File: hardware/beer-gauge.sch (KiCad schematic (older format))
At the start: 10 parts

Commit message: Created TEENSY footprint
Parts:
- added W? (x5): TEST_1P, symbol TEST_1P
- U?: footprint MODULE -> TEENSY:TEENSY
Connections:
- net labels added: TOUCH_DOWN, TOUCH_LEFT, TOUCH_RIGHT, TOUCH_SEL, TOUCH_UP
- wire segments 94 -> 114
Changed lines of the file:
@@
 F 0 "U?" H 3750 2100 50  0000 C CNN
 F 1 "TEENSY_3.2" H 3750 2300 50  0000 C CNN
-F 2 "MODULE" H 3750 2200 50  0001 C CNN
+F 2 "TEENSY:TEENSY" H 3750 2200 50  0001 C CNN
 F 3 "DOCUMENTATION" H 3750 2200 50  0001 C CNN
 	1    3750 2200
@@
 Wire Wire Line
 	8100 2450 8100 2400
-Text Label 1150 1750 0    60   ~ 0
+Text Label 2300 1650 0    60   ~ 0
 SCALE_GAIN0
-Text Label 1150 1850 0    60   ~ 0
+Text Label 2300 1750 0    60   ~ 0
 SCALE_GAIN1
 Text Label 2250 2850 0    60   ~ 0
@@
 Text Label 5300 2750 2    60   ~ 0
 SCALE_SCLK
-Text Label 1150 2150 0    60   ~ 0
+Text Label 2300 1850 0    60   ~ 0
 SCALE_PWDN
-Text Label 1150 2250 0    60   ~ 0
+Text Label 2300 1950 0    60   ~ 0
 SCALE_SPEED
-Text Label 1150 2350 0    60   ~ 0
+Text Label 2300 2050 0    60   ~ 0
 SCALE_A0
-Text Label 1150 2450 0    60   ~ 0
+Text Label 2300 2150 0    60   ~ 0
 SCALE_A1
 Wire Wire Line
@@
 Wire Wire Line
 	4450 5950 4450 5900
-Text Label 1150 2700 0    60   ~ 0
+Text Label 5300 2150 2    60   ~ 0
 DISP_RESET
 Text Label 5300 2250 2    60   ~ 0
@@
 Wire Wire Line
 	4500 2250 5300 2250
+$Comp
+L TEST_1P W?
+U 1 1 575F5A41
+P 7050 5500
+F 0 "W?" H 7050 5770 50  0000 C CNN
+F 1 "TEST_1P" H 7050 5700 50  0000 C CNN
+F 2 "" H 7250 5500 50  0000 C CNN
+F 3 "" H 7250 5500 50  0000 C CNN
+	1    7050 5500
+	0    -1   -1   0
+$EndComp
+$Comp
+L TEST_1P W?
+U 1 1 575F5ABE
+P 6450 6100
+F 0 "W?" H 6450 6370 50  0000 C CNN
+F 1 "TEST_1P" H 6450 6300 50  0000 C CNN
+F 2 "" H 6650 6100 50  0000 C CNN
+F 3 "" H 6650 6100 50  0000 C CNN
+	1    6450 6100
+	1    0    0    -1
+$EndComp
+$Comp
+L TEST_1P W?
+U 1 1 575F5BDB
+P 5800 5500
+F 0 "W?" H 5800 5770 50  0000 C CNN
+F 1 "TEST_1P" H 5800 5700 50  0000 C CNN
+F 2 "" H 6000 5500 50  0000 C CNN
+F 3 "" H 6000 5500 50  0000 C CNN
+	1    5800 5500
+	0    1    1    0
+$EndComp
+$Comp
+L TEST_1P W?
+U 1 1 575F5C18
+P 6550 5500
+F 0 "W?" H 6550 5770 50  0000 C CNN
+F 1 "TEST_1P" H 6550 5700 50  0000 C CNN
+F 2 "" H 6750 5500 50  0000 C CNN
+F 3 "" H 6750 5500 50  0000 C CNN
+	1    6550 5500
+	0    -1   -1   0
+$EndComp
+$Comp
+L TEST_1P W?
+U 1 1 575F5C61
+P 6450 4900
+F 0 "W?" H 6450 5170 50  0000 C CNN
+F 1 "TEST_1P" H 6450 5100 50  0000 C CNN
+F 2 "" H 6650 4900 50  0000 C CNN
+F 3 "" H 6650 4900 50  0000 C CNN
+	1    6450 4900
+	-1   0    0    1
+$EndComp
+Text Label 5200 5500 0    60   ~ 0
+TOUCH_LEFT
+Wire Wire Line
+	5200 5500 5800 5500
+Text Label 7700 5500 2    60   ~ 0
+TOUCH_RIGHT
+Wire Wire Line
+	7050 5500 7700 5500
+Text Label 5900 4850 0    60   ~ 0
+TOUCH_UP
+Wire Wire Line
+	5900 4850 6450 4850
+Wire Wire Line
+	6450 4850 6450 4900
+Text Label 5800 6250 0    60   ~ 0
+TOUCH_DOWN
+Wire Wire Line
+	5800 6250 6450 6250
+Wire Wire Line
+	6450 6250 6450 6100
+Text Label 7150 5300 2    60   ~ 0
+TOUCH_SEL
+Wire Wire Line
+	7150 5300 6550 5300
+Wire Wire Line
+	6550 5300 6550 5500
+Text Label 5300 1850 2    60   ~ 0
+TOUCH_UP
+Text Label 5300 1950 2    60   ~ 0
+TOUCH_DOWN
+Text Label 5300 2450 2    60   ~ 0
+TOUCH_LEFT
+Text Label 5300 2550 2    60   ~ 0
+TOUCH_RIGHT
+Text Label 5300 2650 2    60   ~ 0
+TOUCH_SEL
+Wire Wire Line
+	4500 2450 5300 2450
+Wire Wire Line
+	4500 2550 5300 2550
+Wire Wire Line
+	4500 2650 5300 2650
+Wire Wire Line
+	4500 2150 5300 2150
+Wire Wire Line
+	4500 1850 5300 1850
+Wire Wire Line
+	4500 1950 5300 1950
+Wire Wire Line
+	2300 1650 3000 1650
+Wire Wire Line
+	2300 1750 3000 1750
+Wire Wire Line
+	2300 1850 3000 1850
+Wire Wire Line
+	2300 1950 3000 1950
+Wire Wire Line
+	2300 2050 3000 2050
+Wire Wire Line
+	2300 2150 3000 2150
 $EndSCHEMATC

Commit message: Added subsheet for TEENSY schematic.  Working on TEENSY circuit based on online reference design.
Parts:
- removed U?: TEENSY_3.2, TEENSY:TEENSY, symbol TEENSY_3.2
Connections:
- wire segments 114 -> 134
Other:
- moved on the sheet: C?, IC?, P?, U?, W?

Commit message: Working on schematic
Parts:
- removed W? (x5): TEST_1P, symbol TEST_1P
- added C2: 0.1u, symbol C
- added D1: LED, symbol LED
- added R1: 470, symbol R
- added TP1, TP2, TP3, TP4, TP5: TOUCH_PAD, symbol TOUCH_PAD
- C3: renamed from C?; footprint (none) -> Capacitors_SMD:C_0603
- gave numbers to parts that had none: 8
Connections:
- wire segments 134 -> 110
- no-connect marks 6 -> 5
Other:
- moved on the sheet: C1, C3, C4, P1, P2, P3, P4, U1, U2

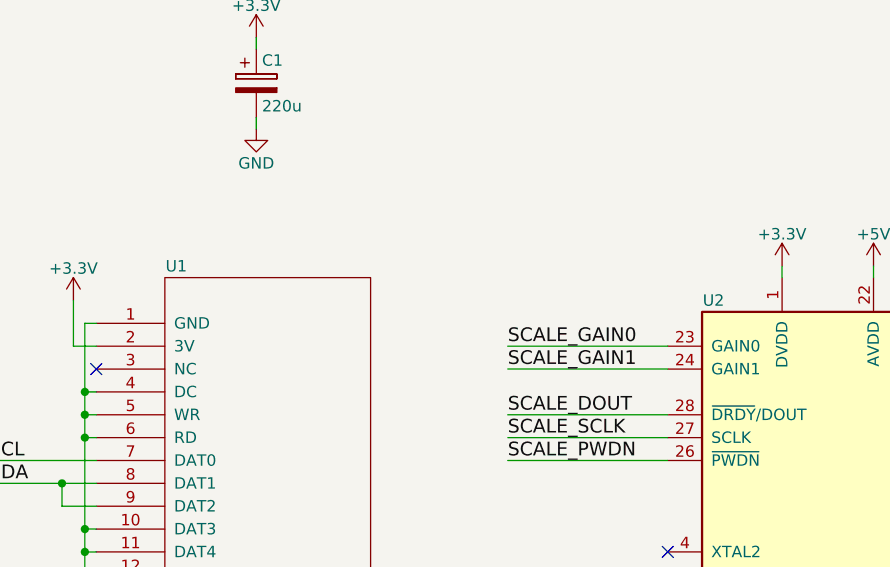
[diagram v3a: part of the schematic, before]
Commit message: Created schematic PDF.  Working on BOM.
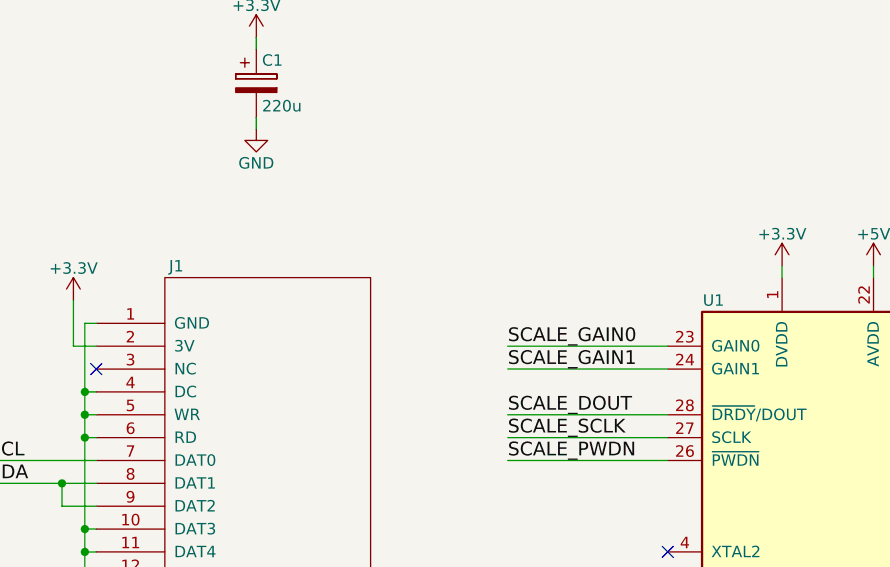
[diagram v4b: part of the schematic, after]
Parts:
- renumbered U1 to J1, U2 to U1
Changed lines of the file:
@@
 $EndDescr
 $Comp
-L ADS1234IPW U2
+L ADS1234IPW U1
 U 1 1 575B8EE8
 P 8000 3300
-F 0 "U2" H 8500 4400 50  0000 C CNN
+F 0 "U1" H 8500 4400 50  0000 C CNN
 F 1 "ADS1234IPW" H 7300 2200 50  0000 L CNN
 F 2 "" H 8000 3300 50  0000 C CIN
@@
 SCALE_A1
 $Comp
-L OLED_MODULE U1
+L OLED_MODULE J1
 U 1 1 575BBA3C
 P 5550 3250
-F 0 "U1" H 5150 4450 50  0000 C CNN
+F 0 "J1" H 5150 4450 50  0000 C CNN
 F 1 "OLED_MODULE" H 5350 2050 50  0000 C CNN
 F 2 "MODULE" H 5550 3250 50  0001 C CNN

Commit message: Working on BOM.
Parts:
- C1: footprint (none) -> Capacitors_SMD:c_elec_6.3x5.8
- C2, C4: footprint (none) -> Capacitors_SMD:C_0603
- D1: footprint (none) -> LEDs:LED_0603
- R1: footprint (none) -> Resistors_SMD:R_0603
- U1: footprint (none) -> Housings_SSOP:TSSOP-28_4.4x9.7mm_Pitch0.65mm
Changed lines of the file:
@@
 F 0 "U1" H 8500 4400 50  0000 C CNN
 F 1 "ADS1234IPW" H 7300 2200 50  0000 L CNN
-F 2 "" H 8000 3300 50  0000 C CIN
+F 2 "Housings_SSOP:TSSOP-28_4.4x9.7mm_Pitch0.65mm" H 8000 3300 50  0001 C CIN
 F 3 "" H 8000 3300 50  0000 C CNN
 	1    8000 3300
@@
 $EndComp
 $Comp
-L +5V #PWR01
+L +5V #PWR16
 U 1 1 575B9063
 P 9600 2400
-F 0 "#PWR01" H 9600 2250 50  0001 C CNN
+F 0 "#PWR16" H 9600 2250 50  0001 C CNN
 F 1 "+5V" H 9600 2540 50  0000 C CNN
 F 2 "" H 9600 2400 50  0000 C CNN
@@
 $EndComp
 $Comp
-L +3.3V #PWR02
+L +3.3V #PWR7
 U 1 1 575B907B
 P 7800 2050
-F 0 "#PWR02" H 7800 1900 50  0001 C CNN
+F 0 "#PWR7" H 7800 1900 50  0001 C CNN
 F 1 "+3.3V" H 7800 2190 50  0000 C CNN
 F 2 "" H 7800 2050 50  0000 C CNN
@@
 $EndComp
 $Comp
-L GND #PWR03
+L GND #PWR8
 U 1 1 575B9093
 P 8000 4600
-F 0 "#PWR03" H 8000 4350 50  0001 C CNN
+F 0 "#PWR8" H 8000 4350 50  0001 C CNN
 F 1 "GND" H 8000 4450 50  0000 C CNN
 F 2 "" H 8000 4600 50  0000 C CNN
@@
 $EndComp
 $Comp
-L GND #PWR04
+L GND #PWR17
 U 1 1 575B9815
 P 9700 4400
-F 0 "#PWR04" H 9700 4150 50  0001 C CNN
+F 0 "#PWR17" H 9700 4150 50  0001 C CNN
 F 1 "GND" H 9700 4250 50  0000 C CNN
 F 2 "" H 9700 4400 50  0000 C CNN
@@
 $EndComp
 $Comp
-L GND #PWR05
+L GND #PWR11
 U 1 1 575B9A5F
 P 8850 4300
-F 0 "#PWR05" H 8850 4050 50  0001 C CNN
+F 0 "#PWR11" H 8850 4050 50  0001 C CNN
 F 1 "GND" H 8850 4150 50  0000 C CNN
 F 2 "" H 8850 4300 50  0000 C CNN
@@
 $EndComp
 $Comp
-L +5V #PWR06
+L +5V #PWR10
 U 1 1 575BA1FA
 P 8750 2300
-F 0 "#PWR06" H 8750 2150 50  0001 C CNN
+F 0 "#PWR10" H 8750 2150 50  0001 C CNN
 F 1 "+5V" H 8750 2440 50  0000 C CNN
 F 2 "" H 8750 2300 50  0000 C CNN
@@
 $EndComp
 $Comp
-L +5V #PWR07
+L +5V #PWR9
 U 1 1 575BA2EA
 P 8200 2050
-F 0 "#PWR07" H 8200 1900 50  0001 C CNN
+F 0 "#PWR9" H 8200 1900 50  0001 C CNN
 F 1 "+5V" H 8200 2190 50  0000 C CNN
 F 2 "" H 8200 2050 50  0000 C CNN
@@
 F 0 "C4" H 9225 1800 50  0000 L CNN
 F 1 "0.1u" H 9225 1600 50  0000 L CNN
-F 2 "" H 9238 1550 50  0000 C CNN
+F 2 "Capacitors_SMD:C_0603" H 9238 1550 50  0001 C CNN
 F 3 "" H 9200 1700 50  0000 C CNN
 	1    9200 1700
@@
 $EndComp
 $Comp
-L +5V #PWR08
+L +5V #PWR14
 U 1 1 575BA474
 P 9200 1500
-F 0 "#PWR08" H 9200 1350 50  0001 C CNN
+F 0 "#PWR14" H 9200 1350 50  0001 C CNN
 F 1 "+5V" H 9200 1640 50  0000 C CNN
 F 2 "" H 9200 1500 50  0000 C CNN
@@
 $EndComp
 $Comp
-L GND #PWR09
+L GND #PWR15
 U 1 1 575BA4B7
 P 9200 1900
-F 0 "#PWR09" H 9200 1650 50  0001 C CNN
+F 0 "#PWR15" H 9200 1650 50  0001 C CNN
 F 1 "GND" H 9200 1750 50  0000 C CNN
 F 2 "" H 9200 1900 50  0000 C CNN
@@
 $EndComp
 $Comp
-L GND #PWR010
+L GND #PWR6
 U 1 1 575BA95F
 P 7250 4300
-F 0 "#PWR010" H 7250 4050 50  0001 C CNN
+F 0 "#PWR6" H 7250 4050 50  0001 C CNN
 F 1 "GND" H 7250 4150 50  0000 C CNN
 F 2 "" H 7250 4300 50  0000 C CNN
@@
 $EndComp
 $Comp
-L GND #PWR011
+L GND #PWR3
 U 1 1 575BBEBC
 P 4750 4300
-F 0 "#PWR011" H 4750 4050 50  0001 C CNN
+F 0 "#PWR3" H 4750 4050 50  0001 C CNN
 F 1 "GND" H 4750 4150 50  0000 C CNN
 F 2 "" H 4750 4300 50  0000 C CNN
@@
 NoConn ~ 4800 2500
 $Comp
-L +3.3V #PWR012
+L +3.3V #PWR2
 U 1 1 575BC1B4
 P 4700 2200
-F 0 "#PWR012" H 4700 2050 50  0001 C CNN
+F 0 "#PWR2" H 4700 2050 50  0001 C CNN
 F 1 "+3.3V" H 4700 2340 50  0000 C CNN
 F 2 "" H 4700 2200 50  0000 C CNN
@@
 F 0 "C1" H 5525 1350 50  0000 L CNN
 F 1 "220u" H 5525 1150 50  0000 L CNN
-F 2 "" H 5538 1100 50  0000 C CNN
+F 2 "Capacitors_SMD:c_elec_6.3x5.8" H 5538 1100 50  0001 C CNN
 F 3 "" H 5500 1250 50  0000 C CNN
 	1    5500 1250
@@
 DISP_RESET
 $Comp
-L +3.3V #PWR013
+L +3.3V #PWR4
 U 1 1 575BD30D
 P 5500 1050
-F 0 "#PWR013" H 5500 900 50  0001 C CNN
+F 0 "#PWR4" H 5500 900 50  0001 C CNN
 F 1 "+3.3V" H 5500 1190 50  0000 C CNN
 F 2 "" H 5500 1050 50  0000 C CNN
@@
 $EndComp
 $Comp
-L GND #PWR014
+L GND #PWR5
 U 1 1 575BD336
 P 5500 1450
-F 0 "#PWR014" H 5500 1200 50  0001 C CNN
+F 0 "#PWR5" H 5500 1200 50  0001 C CNN
 F 1 "GND" H 5500 1300 50  0000 C CNN
 F 2 "" H 5500 1450 50  0000 C CNN
@@
 F 0 "D1" V 1650 5150 50  0000 C CNN
 F 1 "LED" V 1550 5150 50  0000 C CNN
-F 2 "" H 1600 5300 50  0000 C CNN
+F 2 "LEDs:LED_0603" H 1600 5300 50  0001 C CNN
 F 3 "" H 1600 5300 50  0000 C CNN
 	1    1600 5300
@@
 F 0 "R1" H 1700 4900 50  0000 C CNN
 F 1 "470" V 1600 4850 50  0000 C CNN
-F 2 "" V 1530 4850 50  0000 C CNN
+F 2 "Resistors_SMD:R_0603" V 1530 4850 50  0001 C CNN
 F 3 "" H 1600 4850 50  0000 C CNN
 	1    1600 4850
@@
 	1600 5100 1600 5000
 $Comp
-L GND #PWR015
+L GND #PWR1
 U 1 1 5767AC62
 P 1600 5550
-F 0 "#PWR015" H 1600 5300 50  0001 C CNN
+F 0 "#PWR1" H 1600 5300 50  0001 C CNN
 F 1 "GND" H 1600 5400 50  0000 C CNN
 F 2 "" H 1600 5550 50  0000 C CNN
@@
 F 0 "C2" H 8925 1800 50  0000 L CNN
 F 1 "0.1u" H 8925 1600 50  0000 L CNN
-F 2 "" H 8938 1550 50  0000 C CNN
+F 2 "Capacitors_SMD:C_0603" H 8938 1550 50  0001 C CNN
 F 3 "" H 8900 1700 50  0000 C CNN
 	1    8900 1700
@@
 $EndComp
 $Comp
-L GND #PWR016
+L GND #PWR13
 U 1 1 5768007C
 P 8900 1900
-F 0 "#PWR016" H 8900 1650 50  0001 C CNN
+F 0 "#PWR13" H 8900 1650 50  0001 C CNN
 F 1 "GND" H 8900 1750 50  0000 C CNN
 F 2 "" H 8900 1900 50  0000 C CNN
@@
 	8900 1900 8900 1850
 $Comp
-L +3.3V #PWR017
+L +3.3V #PWR12
 U 1 1 57680447
 P 8900 1500
-F 0 "#PWR017" H 8900 1350 50  0001 C CNN
+F 0 "#PWR12" H 8900 1350 50  0001 C CNN
 F 1 "+3.3V" H 8900 1640 50  0000 C CNN
 F 2 "" H 8900 1500 50  0000 C CNN

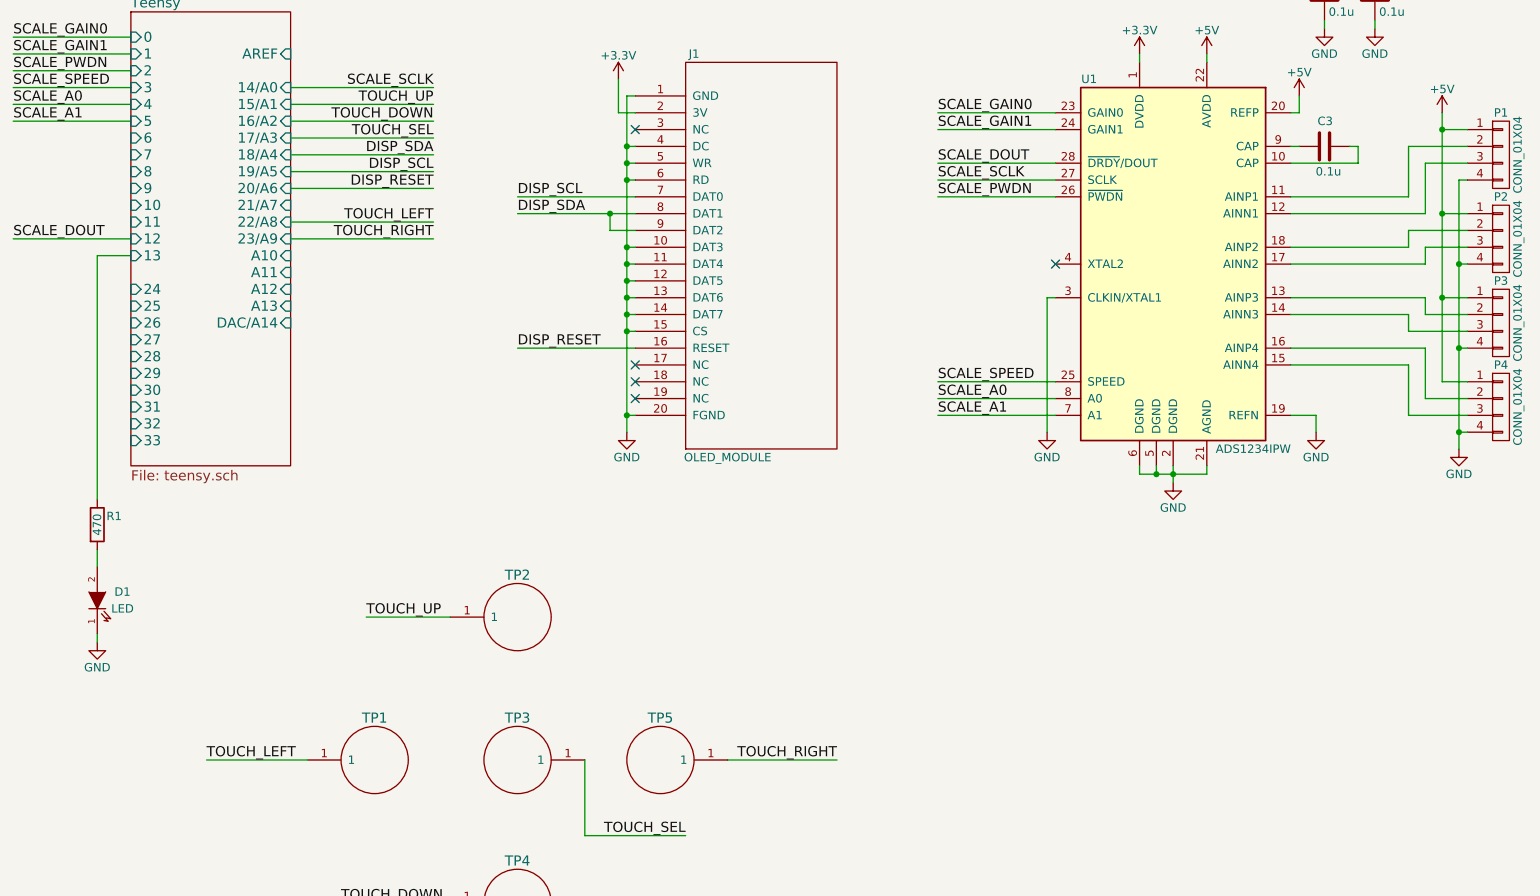
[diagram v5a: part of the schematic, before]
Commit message: Added piezo transducer.  Working on footprints
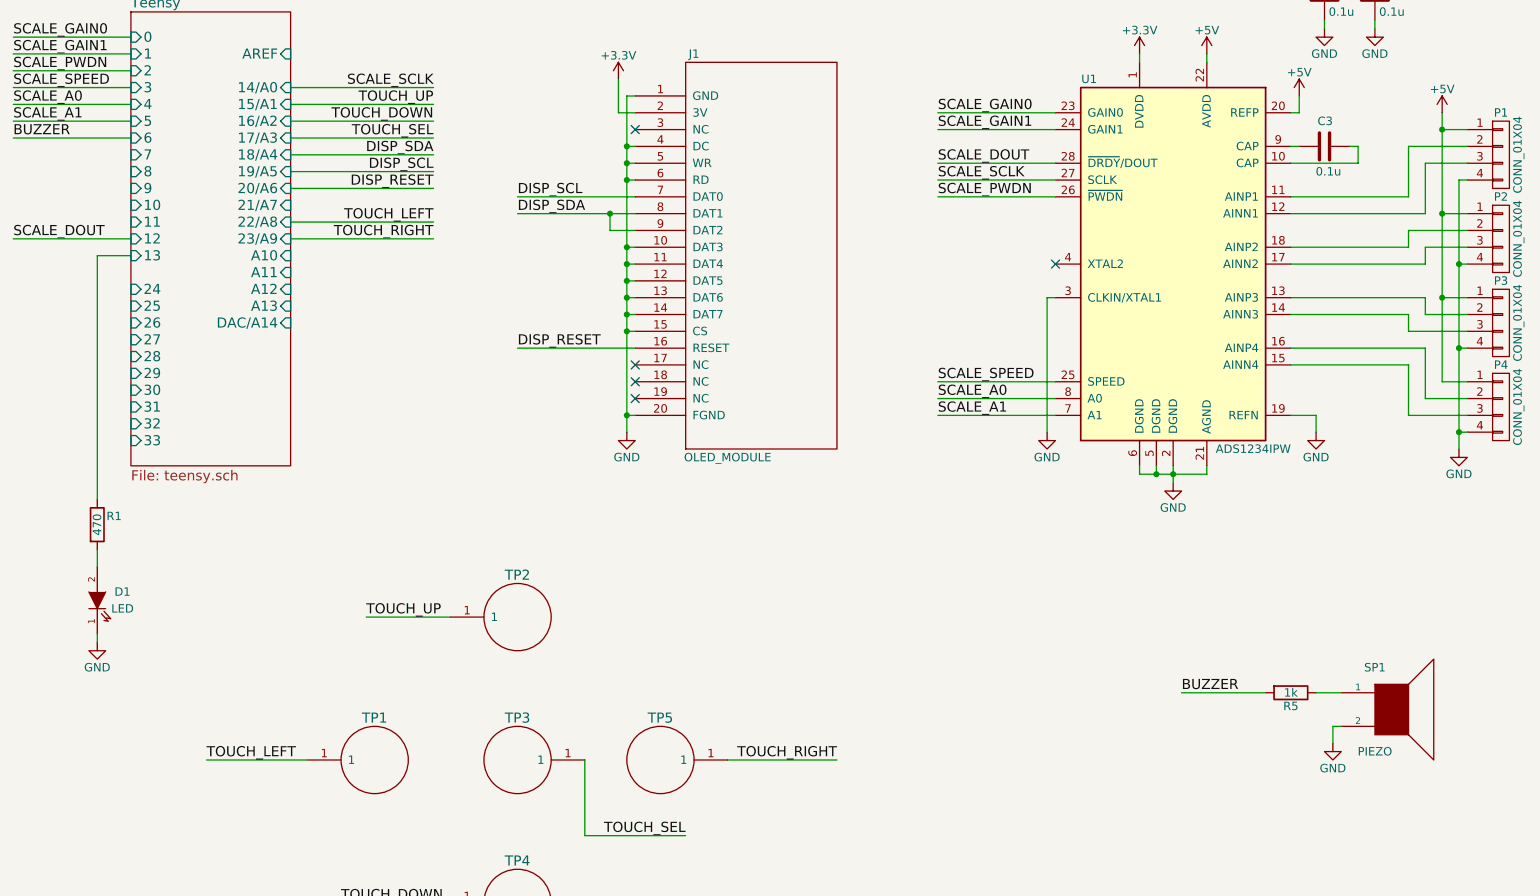
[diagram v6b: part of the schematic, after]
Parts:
- added R5: 1k, symbol R
- added SP1: PIEZO, symbol SPEAKER
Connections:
- net GND: now also SP1.2
- new net: R5.1, SP1.1
- new net BUZZER: R5.2
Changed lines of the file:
@@
 $EndComp
 $Comp
-L +5V #PWR16
+L +5V #PWR17
 U 1 1 575B9063
 P 9600 2400
-F 0 "#PWR16" H 9600 2250 50  0001 C CNN
+F 0 "#PWR17" H 9600 2250 50  0001 C CNN
 F 1 "+5V" H 9600 2540 50  0000 C CNN
 F 2 "" H 9600 2400 50  0000 C CNN
@@
 $EndComp
 $Comp
-L GND #PWR17
+L GND #PWR18
 U 1 1 575B9815
 P 9700 4400
-F 0 "#PWR17" H 9700 4150 50  0001 C CNN
+F 0 "#PWR18" H 9700 4150 50  0001 C CNN
 F 1 "GND" H 9700 4250 50  0000 C CNN
 F 2 "" H 9700 4400 50  0000 C CNN
@@
 $EndComp
 $Comp
-L +5V #PWR14
+L +5V #PWR15
 U 1 1 575BA474
 P 9200 1500
-F 0 "#PWR14" H 9200 1350 50  0001 C CNN
+F 0 "#PWR15" H 9200 1350 50  0001 C CNN
 F 1 "+5V" H 9200 1640 50  0000 C CNN
 F 2 "" H 9200 1500 50  0000 C CNN
@@
 $EndComp
 $Comp
-L GND #PWR15
+L GND #PWR16
 U 1 1 575BA4B7
 P 9200 1900
-F 0 "#PWR15" H 9200 1650 50  0001 C CNN
+F 0 "#PWR16" H 9200 1650 50  0001 C CNN
 F 1 "GND" H 9200 1750 50  0000 C CNN
 F 2 "" H 9200 1900 50  0000 C CNN
@@
 Wire Wire Line
 	8900 1500 8900 1550
+$Comp
+L SPEAKER SP1
+U 1 1 5766D318
+P 9300 5950
+F 0 "SP1" H 9200 6200 50  0000 C CNN
+F 1 "PIEZO" H 9200 5700 50  0000 C CNN
+F 2 "" H 9300 5950 50  0000 C CNN
+F 3 "" H 9300 5950 50  0000 C CNN
+	1    9300 5950
+	1    0    0    -1
+$EndComp
+$Comp
+L R R5
+U 1 1 5766E138
+P 8700 5850
+F 0 "R5" V 8780 5850 50  0000 C CNN
+F 1 "1k" V 8700 5850 50  0000 C CNN
+F 2 "" V 8630 5850 50  0000 C CNN
+F 3 "" H 8700 5850 50  0000 C CNN
+	1    8700 5850
+	0    1    1    0
+$EndComp
+$Comp
+L GND #PWR14
+U 1 1 5766E726
+P 8950 6150
+F 0 "#PWR14" H 8950 5900 50  0001 C CNN
+F 1 "GND" H 8950 6000 50  0000 C CNN
+F 2 "" H 8950 6150 50  0000 C CNN
+F 3 "" H 8950 6150 50  0000 C CNN
+	1    8950 6150
+	1    0    0    -1
+$EndComp
+Wire Wire Line
+	9000 6050 8950 6050
+Wire Wire Line
+	8950 6050 8950 6150
+Wire Wire Line
+	8850 5850 9000 5850
+Text Label 8050 5850 0    60   ~ 0
+BUZZER
+Wire Wire Line
+	8050 5850 8550 5850
+Text Label 1100 2550 0    60   ~ 0
+BUZZER
+Wire Wire Line
+	1100 2550 1800 2550
 $EndSCHEMATC
